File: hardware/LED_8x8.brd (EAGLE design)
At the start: 86 x 82.5 mm, 13 parts, among them IC1 74HC595N, Q1 BC548, Q2 BC548, Q3 BC548, Q4 BC548, Q5 BC548, Q6 BC548, Q7 BC548, Q8 BC548

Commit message: finished layout
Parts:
- IC1: value 74HC595N -> 74HC595D; device 74xx-eu:DIL16 -> 74xx-eu:SO16
- moved IC1 29.0 mm to (43.2, 48.3), flipped to the bottom, turned to 180 degrees
- moved R1 17.8 mm to (30.5, 40.6), flipped to the bottom, turned to 0 degrees
- moved U$2 5.32 mm to (75.2, 25.4)
- moved U$1 3.81 mm to (30.5, 34.3), flipped to the bottom, turned to 0 degrees
- moved U$3 3.81 mm to (30.5, 34.3)
- moved Q1 2.54 mm to (5.08, 68.6), turned to 270 degrees
- moved Q2 2.54 mm to (12.7, 68.6), turned to 270 degrees
- moved Q3 2.54 mm to (20.3, 68.6), turned to 270 degrees
- moved Q4 2.54 mm to (27.9, 68.6), turned to 270 degrees
- moved Q5 2.54 mm to (35.6, 68.6), turned to 270 degrees
- moved Q6 2.54 mm to (43.2, 68.6), turned to 270 degrees
- moved Q7 2.54 mm to (50.8, 68.6), turned to 270 degrees
- moved Q8 2.54 mm to (58.4, 68.6), turned to 270 degrees
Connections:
- removed net VDD: U$2.VUSB
- new net +5V: Q1.C, Q2.C, Q3.C, Q4.C, Q5.C, Q6.C, Q7.C, Q8.C, U$2.VUSB
- net VCC: no longer Q1.C, Q2.C, Q3.C, Q4.C, Q5.C, Q6.C, Q7.C, Q8.C
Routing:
- net +5V: track 0.00 -> 98.9 mm
- net XLAT: track 0.00 -> 72.6 mm, vias 0 -> 2
- net MOSI: track 0.00 -> 68.8 mm
- net SCK: track 0.00 -> 66.0 mm
- net GND: track 20.5 -> 84.9 mm, vias 0 -> 2
- net SHIFTA1: track 0.00 -> 58.8 mm
- net RED1: track 24.2 -> 82.3 mm
- net BLUE8: track 24.2 -> 82.3 mm
- net VCC: track 0.00 -> 54.2 mm, vias 0 -> 4
- net SHIFTA3: track 0.00 -> 50.8 mm
- net RED2: track 24.7 -> 75.1 mm
- net BLUE7: track 24.7 -> 75.1 mm
- net SHIFTA2: track 0.00 -> 49.2 mm
- net BLANK: track 0.00 -> 48.6 mm, vias 0 -> 2
- net RCK: track 0.00 -> 44.5 mm, vias 0 -> 2
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- removed copper zone on layer 1, net N$2
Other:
- board size 86 x 82.5 mm -> 100 x 73.7 mm

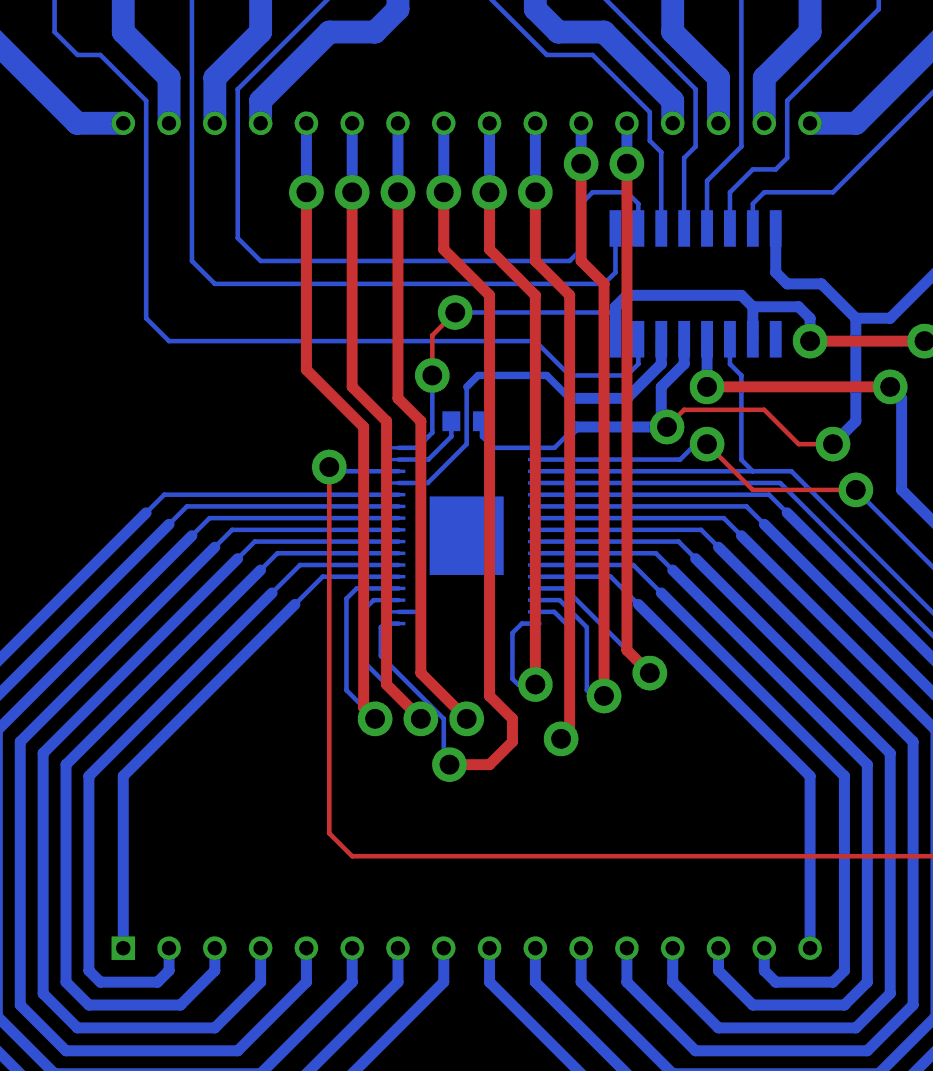
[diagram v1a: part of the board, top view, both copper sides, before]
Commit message: resized drills and vias
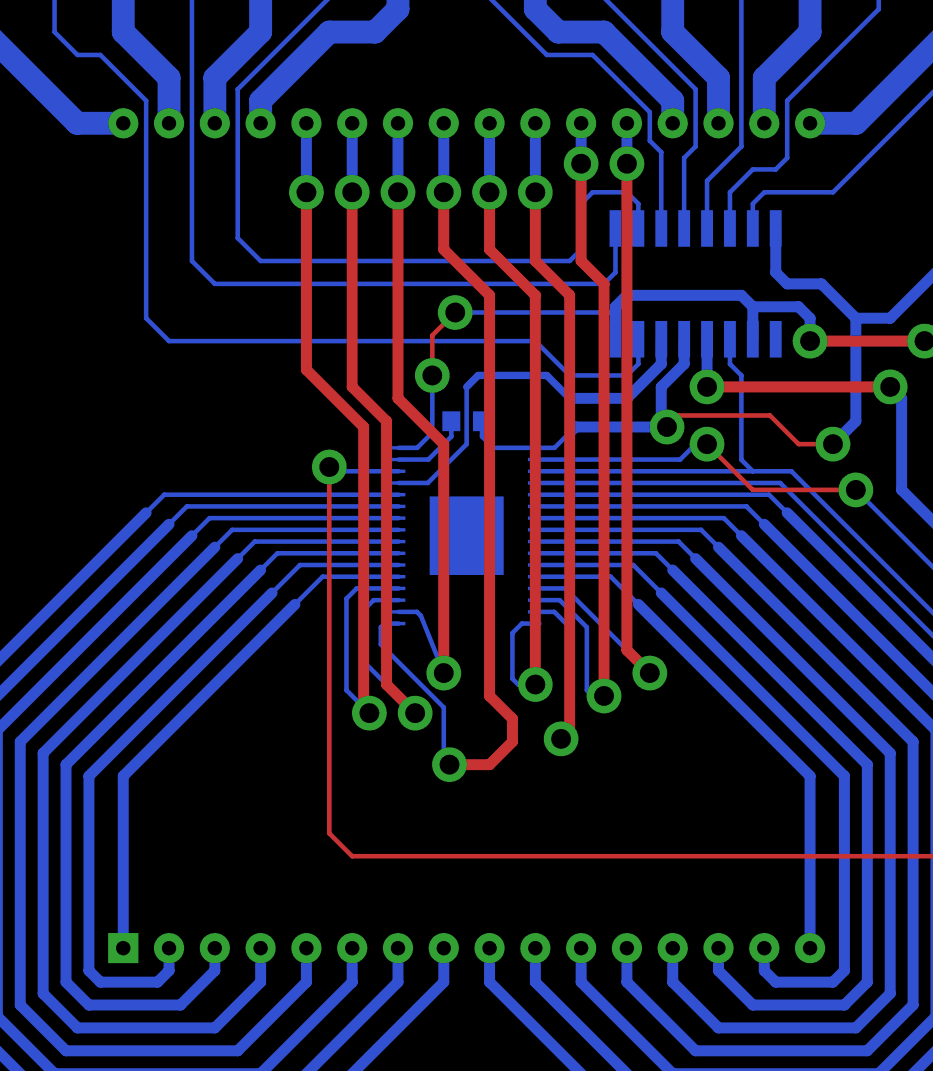
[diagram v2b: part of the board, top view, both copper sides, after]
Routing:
- net GREEN6: track 42.7 -> 36.3 mm
- net GREEN7: track 44.1 -> 43.2 mm
- net GREEN8: track 45.1 -> 44.2 mm
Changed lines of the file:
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@@
 <wire x1="26.705" y1="29.415" x2="25.9225" y2="29.415" width="0.254" layer="16"/>
 <wire x1="25.9225" y1="29.415" x2="25.7175" y2="29.21" width="0.254" layer="16"/>
-<wire x1="25.7175" y1="29.21" x2="25.7175" y2="27.6225" width="0.254" layer="16"/>
-<wire x1="25.7175" y1="27.6225" x2="29.21" y2="24.13" width="0.254" layer="16"/>
-<wire x1="29.21" y1="24.13" x2="29.21" y2="21.9075" width="0.254" layer="16"/>
+<wire x1="25.7175" y1="29.21" x2="25.7175" y2="28.2575" width="0.254" layer="16"/>
+<wire x1="25.7175" y1="28.2575" x2="29.21" y2="24.765" width="0.254" layer="16"/>
+<wire x1="29.21" y1="24.765" x2="29.21" y2="21.9075" width="0.254" layer="16"/>
 <wire x1="29.21" y1="21.9075" x2="29.5275" y2="21.59" width="0.254" layer="16"/>
 <via x="29.5275" y="21.59" extent="1-16" drill="1.1" diameter="1.9304"/>
@@
 <via x="26.67" y="53.34" extent="1-16" drill="1.1" diameter="1.9304"/>
 <wire x1="26.67" y1="53.34" x2="26.67" y2="41.91" width="0.6096" layer="1"/>
-<wire x1="26.67" y1="41.91" x2="27.94" y2="40.64" width="0.6096" layer="1"/>
-<wire x1="27.94" y1="40.64" x2="27.94" y2="26.67" width="0.6096" layer="1"/>
-<wire x1="27.94" y1="26.67" x2="30.48" y2="24.13" width="0.6096" layer="1"/>
+<wire x1="26.67" y1="41.91" x2="29.21" y2="39.37" width="0.6096" layer="1"/>
+<wire x1="29.21" y1="39.37" x2="29.21" y2="26.67" width="0.6096" layer="1"/>
 <wire x1="26.705" y1="30.065" x2="27.72" y2="30.065" width="0.254" layer="16"/>
 <wire x1="27.72" y1="30.065" x2="27.94" y2="29.845" width="0.254" layer="16"/>
-<wire x1="27.94" y1="29.845" x2="27.94" y2="26.67" width="0.254" layer="16"/>
-<wire x1="27.94" y1="26.67" x2="30.48" y2="24.13" width="0.254" layer="16"/>
-<via x="30.48" y="24.13" extent="1-16" drill="1.1" diameter="1.9304"/>
+<wire x1="27.94" y1="29.845" x2="29.21" y2="26.67" width="0.254" layer="16"/>
+<via x="29.21" y="26.67" extent="1-16" drill="1.1" diameter="1.9304"/>
 </signal>
 <signal name="GREEN7">
@@
 <wire x1="24.13" y1="42.545" x2="26.035" y2="40.64" width="0.6096" layer="1"/>
 <wire x1="26.035" y1="40.64" x2="26.035" y2="26.035" width="0.6096" layer="1"/>
-<wire x1="26.035" y1="26.035" x2="27.94" y2="24.13" width="0.6096" layer="1"/>
+<wire x1="26.035" y1="26.035" x2="27.6225" y2="24.4475" width="0.6096" layer="1"/>
 <wire x1="26.705" y1="30.715" x2="25.3175" y2="30.715" width="0.254" layer="16"/>
 <wire x1="25.3175" y1="30.715" x2="24.765" y2="30.1625" width="0.254" layer="16"/>
 <wire x1="24.765" y1="30.1625" x2="24.765" y2="27.305" width="0.254" layer="16"/>
-<wire x1="24.765" y1="27.305" x2="27.94" y2="24.13" width="0.254" layer="16"/>
-<via x="27.94" y="24.13" extent="1-16" drill="1.1" diameter="1.9304"/>
+<wire x1="24.765" y1="27.305" x2="27.6225" y2="24.4475" width="0.254" layer="16"/>
+<via x="27.6225" y="24.4475" extent="1-16" drill="1.1" diameter="1.9304"/>
 </signal>
 <signal name="GREEN8">
@@
 <wire x1="21.59" y1="43.4975" x2="24.765" y2="40.3225" width="0.6096" layer="1"/>
 <wire x1="24.765" y1="40.3225" x2="24.765" y2="24.765" width="0.6096" layer="1"/>
-<wire x1="24.765" y1="24.765" x2="25.4" y2="24.13" width="0.6096" layer="1"/>
-<via x="25.4" y="24.13" extent="1-16" drill="1.1" diameter="1.9304"/>
+<wire x1="24.765" y1="24.765" x2="25.0825" y2="24.4475" width="0.6096" layer="1"/>
+<via x="25.0825" y="24.4475" extent="1-16" drill="1.1" diameter="1.9304"/>
 <wire x1="26.705" y1="31.365" x2="24.38" y2="31.365" width="0.254" layer="16"/>
 <wire x1="24.38" y1="31.365" x2="23.8125" y2="30.7975" width="0.254" layer="16"/>
 <wire x1="23.8125" y1="30.7975" x2="23.8125" y2="25.7175" width="0.254" layer="16"/>
-<wire x1="23.8125" y1="25.7175" x2="25.4" y2="24.13" width="0.254" layer="16"/>
+<wire x1="23.8125" y1="25.7175" x2="25.0825" y2="24.4475" width="0.254" layer="16"/>
 </signal>
 <signal name="BLUE1">
@@
 <wire x1="36.5125" y1="40.3225" x2="41.5925" y2="40.3225" width="0.6096" layer="16"/>
 <wire x1="50.8" y1="39.37" x2="48.895" y2="39.37" width="0.254" layer="1"/>
-<wire x1="48.895" y1="39.37" x2="46.99" y2="41.275" width="0.254" layer="1"/>
-<wire x1="46.99" y1="41.275" x2="42.545" y2="41.275" width="0.254" layer="1"/>
-<wire x1="42.545" y1="41.275" x2="41.5925" y2="40.3225" width="0.254" layer="1"/>
+<wire x1="48.895" y1="39.37" x2="47.3075" y2="40.9575" width="0.254" layer="1"/>
+<wire x1="47.3075" y1="40.9575" x2="42.2275" y2="40.9575" width="0.254" layer="1"/>
+<wire x1="42.2275" y1="40.9575" x2="41.5925" y2="40.3225" width="0.254" layer="1"/>
 <wire x1="42.545" y1="45.1866" x2="42.545" y2="43.815" width="0.6096" layer="16"/>
 <wire x1="42.545" y1="43.815" x2="41.275" y2="42.545" width="0.6096" layer="16"/>

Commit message: minor corrections
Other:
- board size 100 x 73.7 mm -> 85.4 x 73.7 mm
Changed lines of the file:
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@@
 <layer number="37" name="tTest" color="7" fill="1" visible="no" active="yes"/>
 <layer number="38" name="bTest" color="7" fill="1" visible="no" active="yes"/>
-<layer number="39" name="tKeepout" color="4" fill="11" visible="yes" active="yes"/>
-<layer number="40" name="bKeepout" color="1" fill="11" visible="yes" active="yes"/>
-<layer number="41" name="tRestrict" color="4" fill="10" visible="yes" active="yes"/>
-<layer number="42" name="bRestrict" color="1" fill="10" visible="yes" active="yes"/>
-<layer number="43" name="vRestrict" color="2" fill="10" visible="yes" active="yes"/>
+<layer number="39" name="tKeepout" color="4" fill="11" visible="no" active="yes"/>
+<layer number="40" name="bKeepout" color="1" fill="11" visible="no" active="yes"/>
+<layer number="41" name="tRestrict" color="4" fill="10" visible="no" active="yes"/>
+<layer number="42" name="bRestrict" color="1" fill="10" visible="no" active="yes"/>
+<layer number="43" name="vRestrict" color="2" fill="10" visible="no" active="yes"/>
 <layer number="44" name="Drills" color="7" fill="1" visible="no" active="yes"/>
 <layer number="45" name="Holes" color="7" fill="1" visible="no" active="yes"/>
 <layer number="46" name="Milling" color="3" fill="1" visible="no" active="yes"/>
 <layer number="47" name="Measures" color="7" fill="1" visible="no" active="yes"/>
-<layer number="48" name="Document" color="7" fill="1" visible="yes" active="yes"/>
-<layer number="49" name="Reference" color="7" fill="1" visible="yes" active="yes"/>
+<layer number="48" name="Document" color="7" fill="1" visible="no" active="yes"/>
+<layer number="49" name="Reference" color="7" fill="1" visible="no" active="yes"/>
 <layer number="50" name="dxf" color="7" fill="1" visible="no" active="no"/>
-<layer number="51" name="tDocu" color="7" fill="1" visible="yes" active="yes"/>
-<layer number="52" name="bDocu" color="7" fill="1" visible="yes" active="yes"/>
+<layer number="51" name="tDocu" color="7" fill="1" visible="no" active="yes"/>
+<layer number="52" name="bDocu" color="7" fill="1" visible="no" active="yes"/>
 <layer number="53" name="tGND_GNDA" color="7" fill="1" visible="no" active="no"/>
 <layer number="54" name="bGND_GNDA" color="7" fill="1" visible="no" active="no"/>
@@
 <layer number="98" name="Guide" color="6" fill="1" visible="no" active="no"/>
 <layer number="99" name="Anatomie" color="7" fill="1" visible="no" active="no"/>
-<layer number="100" name="Muster" color="7" fill="1" visible="yes" active="yes"/>
-<layer number="101" name="Patch_Top" color="7" fill="1" visible="yes" active="yes"/>
-<layer number="102" name="Brücken" color="7" fill="1" visible="yes" active="yes"/>
-<layer number="103" name="CableCode" color="7" fill="1" visible="yes" active="yes"/>
+<layer number="100" name="Muster" color="7" fill="1" visible="no" active="yes"/>
+<layer number="101" name="Patch_Top" color="7" fill="1" visible="no" active="yes"/>
+<layer number="102" name="Brücken" color="7" fill="1" visible="no" active="yes"/>
+<layer number="103" name="CableCode" color="7" fill="1" visible="no" active="yes"/>
 <layer number="104" name="Name" color="7" fill="1" visible="no" active="yes"/>
 <layer number="105" name="Beschreib" color="9" fill="1" visible="no" active="yes"/>
@@
 <layer number="108" name="fp8" color="7" fill="1" visible="no" active="yes"/>
 <layer number="109" name="fp9" color="7" fill="1" visible="no" active="yes"/>
-<layer number="110" name="tdokum" color="7" fill="1" visible="yes" active="yes"/>
-<layer number="111" name="bdokum" color="7" fill="1" visible="yes" active="yes"/>
-<layer number="116" name="Patch_BOT" color="7" fill="1" visible="yes" active="yes"/>
+<layer number="110" name="tdokum" color="7" fill="1" visible="no" active="yes"/>
+<layer number="111" name="bdokum" color="7" fill="1" visible="no" active="yes"/>
+<layer number="116" name="Patch_BOT" color="7" fill="1" visible="no" active="yes"/>
 <layer number="121" name="_tsilk" color="7" fill="1" visible="no" active="yes"/>
 <layer number="122" name="_bsilk" color="7" fill="1" visible="no" active="yes"/>
 <layer number="123" name="tTestmark" color="7" fill="1" visible="no" active="yes"/>
 <layer number="124" name="bTestmark" color="7" fill="1" visible="no" active="yes"/>
-<layer number="125" name="_tNames" color="7" fill="1" visible="yes" active="yes"/>
-<layer number="126" name="_bNames" color="7" fill="1" visible="yes" active="yes"/>
+<layer number="125" name="_tNames" color="7" fill="1" visible="no" active="yes"/>
+<layer number="126" name="_bNames" color="7" fill="1" visible="no" active="yes"/>
 <layer number="131" name="tAdjust" color="7" fill="1" visible="no" active="yes"/>
 <layer number="132" name="bAdjust" color="7" fill="1" visible="no" active="yes"/>
 <layer number="144" name="Drill_legend" color="7" fill="1" visible="no" active="yes"/>
 <layer number="151" name="HeatSink" color="7" fill="1" visible="no" active="yes"/>
-<layer number="199" name="L$199" color="7" fill="1" visible="yes" active="yes"/>
-<layer number="200" name="200bmp" color="7" fill="1" visible="yes" active="yes"/>
-<layer number="201" name="201bmp" color="7" fill="1" visible="yes" active="yes"/>
-<layer number="202" name="202bmp" color="7" fill="1" visible="yes" active="yes"/>
+<layer number="199" name="L$199" color="7" fill="1" visible="no" active="yes"/>
+<layer number="200" name="200bmp" color="7" fill="1" visible="no" active="yes"/>
+<layer number="201" name="201bmp" color="7" fill="1" visible="no" active="yes"/>
+<layer number="202" name="202bmp" color="7" fill="1" visible="no" active="yes"/>
 <layer number="203" name="203bmp" color="4" fill="10" visible="no" active="yes"/>
 <layer number="204" name="204bmp" color="5" fill="10" visible="no" active="yes"/>
@@
 <layer number="215" name="215bmp" color="7" fill="1" visible="no" active="yes"/>
 <layer number="216" name="216bmp" color="7" fill="1" visible="no" active="yes"/>
-<layer number="250" name="Descript" color="7" fill="1" visible="yes" active="yes"/>
-<layer number="251" name="SMDround" color="7" fill="1" visible="yes" active="yes"/>
-<layer number="254" name="Cool" color="7" fill="1" visible="yes" active="yes"/>
+<layer number="250" name="Descript" color="7" fill="1" visible="no" active="yes"/>
+<layer number="251" name="SMDround" color="7" fill="1" visible="no" active="yes"/>
+<layer number="254" name="Cool" color="7" fill="1" visible="no" active="yes"/>
 </layers>
 <board>
 <plain>
-<wire x1="0" y1="0" x2="100" y2="0" width="0" layer="20"/>
-<wire x1="100" y1="0" x2="100" y2="73.65" width="0" layer="20"/>
-<wire x1="100" y1="73.65" x2="0" y2="73.65" width="0" layer="20"/>
+<wire x1="0" y1="0" x2="85.395" y2="0" width="0" layer="20"/>
+<wire x1="85.395" y1="0" x2="85.395" y2="73.65" width="0" layer="20"/>
+<wire x1="85.395" y1="73.65" x2="0" y2="73.65" width="0" layer="20"/>
 <wire x1="0" y1="73.65" x2="0" y2="0" width="0" layer="20"/>
 </plain>
